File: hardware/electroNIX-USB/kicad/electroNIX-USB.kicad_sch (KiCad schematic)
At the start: 4 parts

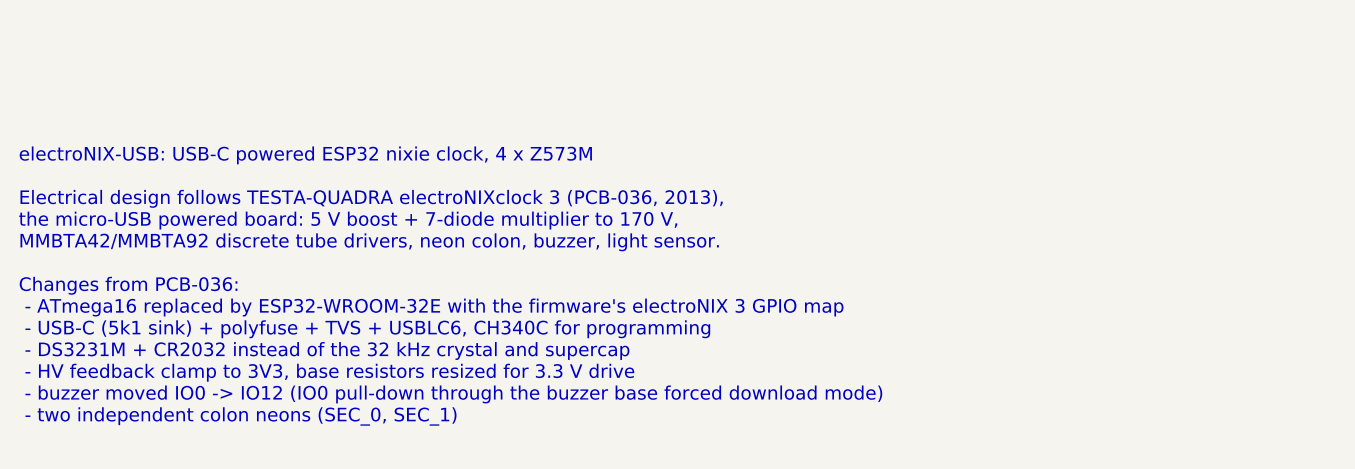
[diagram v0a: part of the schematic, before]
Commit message: electroNIX-USB: add 6-tube variant
The generator takes --tubes 4|6. The 6-tube build adds two anode switches
on IO12/IO15 and doubles the colon neons. It drops the buzzer and DS3231,
which matches the stock BOARD_ELECTRONIX_4_6T GPIO map, so no firmware
change is needed. HV supply, cathode drivers, ESP32, USB and power are
unchanged. Both projects are committed, with their own schematic PDF
and BOM.

Co-Authored-By: Claude Opus 5.5 <noreply@anthropic.com>
Claude-Session: https://claude.ai/code/session_01AFMfevKEKDGbci8uJGhf4W
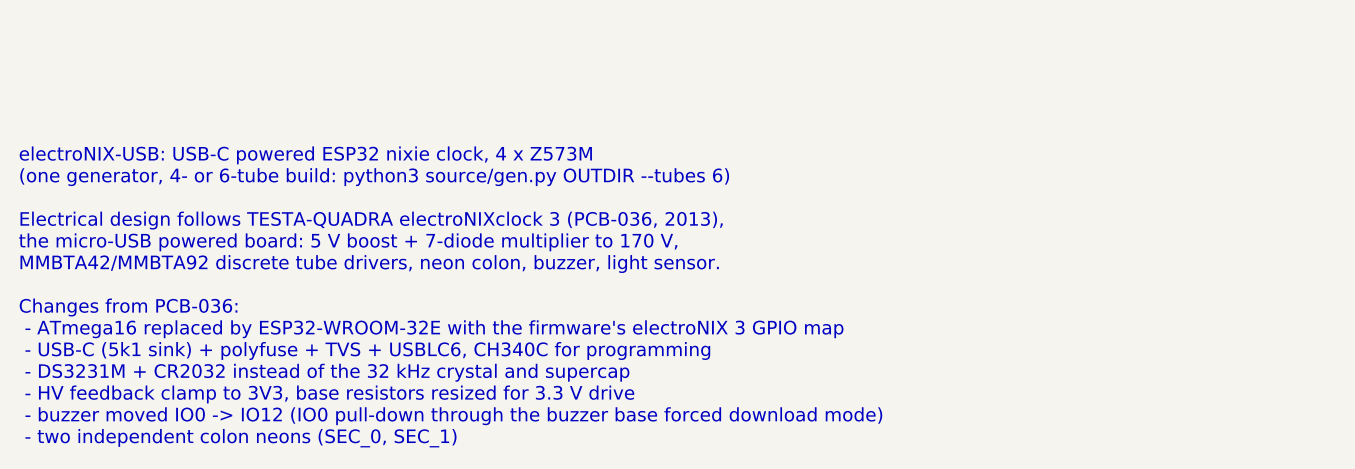
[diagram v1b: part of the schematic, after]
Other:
- note added: "electroNIX-USB: USB-C powered ESP32 nixie clock, 4 x Z573M (one generator, 4- or 6-tube build: python3 source/gen.py OUTDIR --tubes 6) Electrical design follows TESTA-QUADRA electroNIXclock 3 (PCB-036, 2013), the micro-USB powered board: 5 V boost + 7-diode multiplier to 170 V, MMBTA42/MMBTA92 discrete tube drivers, neon colon, buzzer, light sensor. Changes from PCB-036: - ATmega16 replaced by ES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"
- note removed: "electroNIX-USB: USB-C powered ESP32 nixie clock, 4 x Z573M Electrical design follows TESTA-QUADRA electroNIXclock 3 (PCB-036, 2013), the micro-USB powered board: 5 V boost + 7-diode multiplier to 170 V, MMBTA42/MMBTA92 discrete tube drivers, neon colon, buzzer, light sensor. Changes from PCB-036: - ATmega16 replaced by ESP32-WROOM-32E with the firmware's electroNIX 3 GPIO map - USB-C (5k1 sink) +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"
- title: electroNIX-USB (Z573M) - overview -> electroNIX-USB (Z573M, 4 tubes) - overview
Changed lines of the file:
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@@
   (paper "A3")
   (title_block
-    (title "electroNIX-USB (Z573M) - overview")
+    (title "electroNIX-USB (Z573M, 4 tubes) - overview")
     (date "2026-10-15")
     (rev "0.1")
@@
     (comment 1 "ESP32 rework of TESTA-QUADRA electroNIXclock 3 (PCB-036), USB powered")
     (comment 2 "Licensed with the repository; see LICENSE"))
-  (text "electroNIX-USB: USB-C powered ESP32 nixie clock, 4 x Z573M\n\nElectrical design follows TESTA-QUADRA electroNIXclock 3 (PCB-036, 2013),\nthe micro-USB powered board: 5 V boost + 7-diode multiplier to 170 V,\nMMBTA42/MMBTA92 discrete tube drivers, neon colon, buzzer, light sensor.\n\nChanges from PCB-036:\n - ATmega16 replaced by ESP32-WROOM-32E with the firmware's electroNIX 3 GPIO map\n - USB-C (5k1 sink) + polyfuse + TVS + USBLC6, CH340C for programming\n - DS3231M + CR2032 instead of the 32 kHz crystal and supercap\n - HV feedback clamp to 3V3, base resistors resized for 3.3 V drive\n - buzzer moved IO0 -> IO12 (IO0 pull-down through the buzzer base forced download mode)\n - two independent colon neons (SEC_0, SEC_1)"
+  (text "electroNIX-USB: USB-C powered ESP32 nixie clock, 4 x Z573M\n(one generator, 4- or 6-tube build: python3 source/gen.py OUTDIR --tubes 6)\n\nElectrical design follows TESTA-QUADRA electroNIXclock 3 (PCB-036, 2013),\nthe micro-USB powered board: 5 V boost + 7-diode multiplier to 170 V,\nMMBTA42/MMBTA92 discrete tube drivers, neon colon, buzzer, light sensor.\n\nChanges from PCB-036:\n - ATmega16 replaced by ESP32-WROOM-32E with the firmware's electroNIX 3 GPIO map\n - USB-C (5k1 sink) + polyfuse + TVS + USBLC6, CH340C for programming\n - DS3231M + CR2032 instead of the 32 kHz crystal and supercap\n - HV feedback clamp to 3V3, base resistors resized for 3.3 V drive\n - buzzer moved IO0 -> IO12 (IO0 pull-down through the buzzer base forced download mode)\n - two independent colon neons (SEC_0, SEC_1)"
     (at 30 180 0)
     (effects

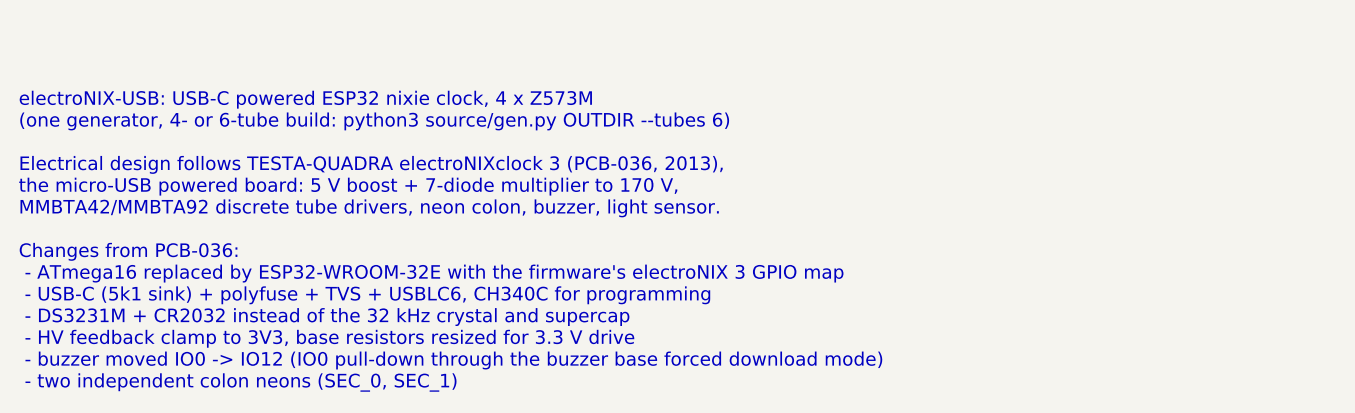
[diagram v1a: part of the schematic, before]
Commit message: electroNIX-USB: drop buzzer and DS3231, run stock firmware
Both builds now match a stock firmware profile with no changes:
BOARD_ELECTRONIX_3 for 4 tubes, BOARD_ELECTRONIX_4_6T for 6 tubes. Time
comes from NTP. IO0 gets a plain 10k pull-up. On the 4-tube build IO12
and IO15 are left open and reserved for anodes 5/6.

Co-Authored-By: Claude Opus 5.5 <noreply@anthropic.com>
Claude-Session: https://claude.ai/code/session_01AFMfevKEKDGbci8uJGhf4W
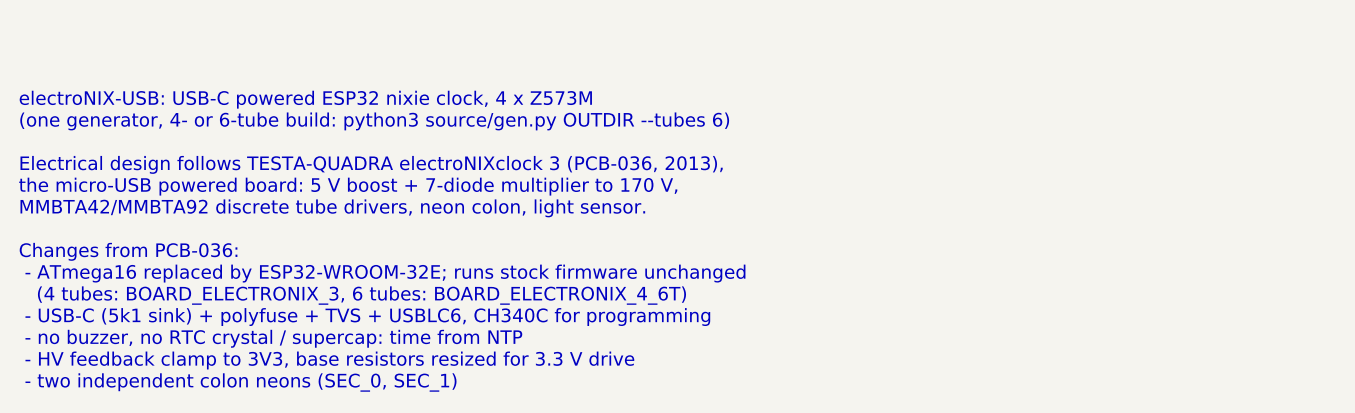
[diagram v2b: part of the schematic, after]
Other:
- note added: "electroNIX-USB: USB-C powered ESP32 nixie clock, 4 x Z573M (one generator, 4- or 6-tube build: python3 source/gen.py OUTDIR --tubes 6) Electrical design follows TESTA-QUADRA electroNIXclock 3 (PCB-036, 2013), the micro-USB powered board: 5 V boost + 7-diode multiplier to 170 V, MMBTA42/MMBTA92 discrete tube drivers, neon colon, light sensor. Changes from PCB-036: - ATmega16 replaced by ESP32-WROO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"
- note removed: "electroNIX-USB: USB-C powered ESP32 nixie clock, 4 x Z573M (one generator, 4- or 6-tube build: python3 source/gen.py OUTDIR --tubes 6) Electrical design follows TESTA-QUADRA electroNIXclock 3 (PCB-036, 2013), the micro-USB powered board: 5 V boost + 7-diode multiplier to 170 V, MMBTA42/MMBTA92 discrete tube drivers, neon colon, buzzer, light sensor. Changes from PCB-036: - ATmega16 replaced by ES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"
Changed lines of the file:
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@@
     (comment 1 "ESP32 rework of TESTA-QUADRA electroNIXclock 3 (PCB-036), USB powered")
     (comment 2 "Licensed with the repository; see LICENSE"))
-  (text "electroNIX-USB: USB-C powered ESP32 nixie clock, 4 x Z573M\n(one generator, 4- or 6-tube build: python3 source/gen.py OUTDIR --tubes 6)\n\nElectrical design follows TESTA-QUADRA electroNIXclock 3 (PCB-036, 2013),\nthe micro-USB powered board: 5 V boost + 7-diode multiplier to 170 V,\nMMBTA42/MMBTA92 discrete tube drivers, neon colon, buzzer, light sensor.\n\nChanges from PCB-036:\n - ATmega16 replaced by ESP32-WROOM-32E with the firmware's electroNIX 3 GPIO map\n - USB-C (5k1 sink) + polyfuse + TVS + USBLC6, CH340C for programming\n - DS3231M + CR2032 instead of the 32 kHz crystal and supercap\n - HV feedback clamp to 3V3, base resistors resized for 3.3 V drive\n - buzzer moved IO0 -> IO12 (IO0 pull-down through the buzzer base forced download mode)\n - two independent colon neons (SEC_0, SEC_1)"
+  (text "electroNIX-USB: USB-C powered ESP32 nixie clock, 4 x Z573M\n(one generator, 4- or 6-tube build: python3 source/gen.py OUTDIR --tubes 6)\n\nElectrical design follows TESTA-QUADRA electroNIXclock 3 (PCB-036, 2013),\nthe micro-USB powered board: 5 V boost + 7-diode multiplier to 170 V,\nMMBTA42/MMBTA92 discrete tube drivers, neon colon, light sensor.\n\nChanges from PCB-036:\n - ATmega16 replaced by ESP32-WROOM-32E; runs stock firmware unchanged\n   (4 tubes: BOARD_ELECTRONIX_3, 6 tubes: BOARD_ELECTRONIX_4_6T)\n - USB-C (5k1 sink) + polyfuse + TVS + USBLC6, CH340C for programming\n - no buzzer, no RTC crystal / supercap: time from NTP\n - HV feedback clamp to 3V3, base resistors resized for 3.3 V drive\n - two independent colon neons (SEC_0, SEC_1)"
     (at 30 180 0)
     (effects
